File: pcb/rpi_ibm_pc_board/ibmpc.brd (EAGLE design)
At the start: 56 x 65 mm, 31 parts, among them IC1 STM32F072C8T6, SW4 324_SW, U1 MAX3232

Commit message: clean up
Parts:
- added R10, R7, R8, R9: 2K, SparkFun-Passives:0805
- added R3, R4: 5.1k, SparkFun-Passives:0805
- added R5: 12K, SparkFun-Passives:0805
- added SW1: 324_SW, 3pos_slide_switch_centered:342_SWICH_FOOT
- added U$6: MCP4451, ps2:TSSOP20
- moved JP4 41.8 mm to (51.7, 53.9), turned to 0 degrees
- moved C2 30.0 mm to (10.9, 20.0)
- moved SW4 27.5 mm to (14.7, 38.5), turned to 180 degrees
- moved C3 21.4 mm to (12.1, 9.98)
- moved C1 15.1 mm to (15.4, 17.9)
- moved R1 14.9 mm to (9.19, 16.4)
- moved J3 9.50 mm to (52.0, 23.0)
- moved J4 8.18 mm to (48.0, 45.1)
- moved U1 6.23 mm to (40.4, 24.7), turned to 270 degrees
- moved IC1 2.02 mm to (29.1, 36.7), turned to 270 degrees
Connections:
- new net +UB: R10.2, R7.2, R8.2, R9.2, U$1.1, U$1.8, U$1.9
- new net N$1: J4.A5, R3.1
- new net N$12: IC1.31, JP4.3
- new net N$14: IC1.30, JP4.4
- new net N$15: IC1.34, JP4.1
- new net N$16: IC1.37, JP4.2
- new net N$17: R7.1, U$1.2
- new net N$18: IC1.44, R5.2, SW1.P$1, SW1.P$4
- new net N$19: R8.1, U$1.7
- new net N$20: R9.1, U$1.10
- new net N$21: R10.1, U$1.14
- new net N$7: J4.B5, R4.1
- new net N$8: IC1.33, J4.A6, J4.B6
- new net N$9: IC1.32, J4.A7, J4.B7
- new net SPI_CS: IC1.14, JP1.24
- new net SPI_MISO: IC1.16, JP1.21
- new net SPI_MOSI: IC1.17, JP1.19
- new net SPI_SCK: IC1.15, JP1.23
- net +3V3: now also JP4.6, SW1.P$2, SW1.P$3
- net GND: now also J4.GND, J4.GND2, J4.SHLD1, J4.SHLD2, J4.SHLD3, J4.SHLD4, J4.SHLD5, J4.SHLD6, J4.SHLD7, J4.SHLD8, JP4.5, R3.2, R4.2, R5.1, U$1.4, U$1.5
- net N$13: now also IC1.7

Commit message: working on IBM PC p board
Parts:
- moved R4 81.5 mm to (53.9, 46.4), turned to 180 degrees
- moved R3 77.0 mm to (50.4, 46.4), turned to 180 degrees
- moved R2 72.8 mm to (64.6, 75.2)
- moved LED1 72.8 mm to (64.5, 72.7)
- moved LED2 72.8 mm to (65.7, 62.7)
- moved R6 72.8 mm to (69.8, 62.7)
- moved R5 64.6 mm to (12.2, 47.5), turned to 180 degrees
- moved C3 34.9 mm to (17.6, 44.4), turned to 270 degrees
- moved C2 29.0 mm to (27.5, 43.8), turned to 270 degrees
- moved C6 24.6 mm to (32.4, 35.8), turned to 180 degrees
- moved R1 20.8 mm to (12.2, 37.0), turned to 0 degrees
- moved C9 20.1 mm to (30.0, 32.6), turned to 270 degrees
- moved JP4 19.5 mm to (35.7, 42.8), turned to 270 degrees
- moved C1 19.4 mm to (26.6, 33.7), turned to 270 degrees
- moved C4 18.6 mm to (30.0, 29.6), turned to 270 degrees
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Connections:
- removed net VBAT: IC1.1
- removed net VDDA: IC1.9
- removed net VDD_1: IC1.24
- removed net VDD_2: IC1.36
- removed net VDD_3: IC1.48
- removed net VSSA: IC1.8
- removed net VSS_1: IC1.23
- removed net VSS_2: IC1.35
- removed net VSS_3: IC1.47
- new net N$22: IC1.42, JP1.5
- new net N$23: IC1.43, JP1.3
- new net N$24: IC1.25, U1.10
- new net N$25: J3.8, U1.7
- new net PC_RTS: IC1.19, U1.9
- new net RTS_HV: J3.7, U1.8
- new net STM32_RX: IC1.22, U1.12
- new net STM32_RX_HV: J3.3, U1.13
- new net STM32_TX: IC1.21, U1.11
- new net STM32_TX_HV: J3.2, U1.14
- net +3V3: now also IC1.1, IC1.24, IC1.36, IC1.48, IC1.9, JP4.4; no longer JP4.6
- net GND: now also IC1.23, IC1.35, IC1.47, IC1.8, JP4.3; no longer JP4.5
- net N$12: now also JP4.5; no longer JP4.3
- net N$13: now also JP1.22
- net N$14: now also JP4.6; no longer JP4.4
- net N$18: now also JP1.32
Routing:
- net N$24: track 0.00 -> 52.8 mm
- net GND: track 0.00 -> 32.8 mm
- net RTS_HV: track 0.00 -> 31.5 mm
- net N$9: track 0.00 -> 31.3 mm
- net N$25: track 0.00 -> 31.0 mm
- net N$8: track 0.00 -> 30.5 mm
- net STM32_TX: track 0.00 -> 26.0 mm
- net STM32_RX: track 0.00 -> 25.7 mm
- net PC_RTS: track 0.00 -> 24.7 mm
- net SPI_MOSI: track 0.00 -> 22.1 mm
- net N$18: track 0.00 -> 21.3 mm
- net SPI_SCK: track 0.00 -> 20.5 mm
- net SPI_MISO: track 0.00 -> 20.4 mm
- net +3V3: track 0.00 -> 18.8 mm, vias 0 -> 4
- net SPI_CS: track 0.00 -> 17.1 mm
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
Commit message: ibm card done
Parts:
- removed JP11, JP2, JP3, JP9: (no value), pinhead:1X04
- added C8: 100nF, clock:0805@1
- added LED3: (no value), adafruit:CHIP-LED0805
- added R11, R12: 2K, SparkFun-Passives:0805
- added TP1, TP2, TP3, TP4: TPTP12R, testpad:TP12R
- added U$7, U$8, U$9: PINHD1X4, adafruit_changed:1X04-CLEANBIG
- JP4: device pinhead:2X03 -> pinhead:2X04
- moved R6 56.4 mm to (50.2, 9.83), turned to 270 degrees
- moved LED2 54.5 mm to (52.7, 9.78), turned to 180 degrees
- moved R2 47.5 mm to (26.5, 46.7), turned to 0 degrees
- moved LED1 44.8 mm to (26.5, 49.0)
- moved JP4 2.51 mm to (38.1, 43.4)
- moved U$6 2.44 mm to (18.4, 24.9), turned to 180 degrees
- moved C6 1.94 mm to (34.4, 36.0), turned to 0 degrees
- moved R9 1.02 mm to (23.4, 13.8)
- moved C7 0.92 mm to (40.0, 34.4), turned to 90 degrees
- moved R7 0.70 mm to (19.1, 13.8)
- moved R8 0.68 mm to (38.1, 13.8)
- moved R10 0.57 mm to (34.5, 13.8), turned to 180 degrees
- moved R5 0.51 mm to (12.2, 48.0)
- moved SW1 0.51 mm to (12.2, 45.1)
- moved SW4 0.51 mm to (12.2, 40.4)
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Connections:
- new net N$26: IC1.40, J1.1_DATA, U$7.2
- new net N$27: IC1.38, JP4.1, R11.1
- new net N$28: LED3.A, R11.2
- new net N$30: IC1.27, U$6.6
- new net N$31: IC1.26, U$6.5
- new net N$32: R12.1, U$6.4
- new net N$33: U$1.3, U$6.12
- new net N$34: U$1.11, U$6.9
- new net N$35: U$1.6, U$6.19
- new net N$36: U$1.13, U$6.2
- new net N$37: IC1.2, JP1.36
- new net N$38: IC1.10, U$9.1
- new net N$39: IC1.11, U$9.2
- new net N$40: IC1.12, U$9.3
- new net N$41: IC1.13, U$9.4
- new net N$42: IC1.29, TP1.TP
- new net N$43: IC1.28, TP2.TP
- new net N$44: IC1.20, TP4.TP
- new net N$45: IC1.18, TP3.TP
- net +3V3: now also C8.2, JP4.6, U$6.17; no longer JP11.1, JP11.2, JP11.3, JP11.4, JP4.4, LED1.A
- net +UB: now also U$6.1, U$6.10, U$6.11, U$6.20
- net GND: now also C8.1, JP4.5, LED1.C, LED3.C, R12.2, U$1.G1, U$1.G2, U$6.16, U$6.7, U$7.4, U$8.4; no longer JP2.1, JP3.1, JP4.3, JP9.1, JP9.2, JP9.3, JP9.4
- net N$10: now also IC1.45, U$8.2; no longer JP3.3
- net N$11: now also IC1.46, U$8.3; no longer JP3.2
- net N$12: now also JP4.7; no longer JP4.5
- net N$14: now also JP4.8; no longer JP4.6
- net N$15: now also JP4.3; no longer JP4.1
- net N$16: now also JP4.4; no longer JP4.2
- net N$17: now also IC1.3
- net N$19: now also IC1.5
- net N$2: now also LED1.A; no longer LED1.C
- net N$20: now also IC1.4
- net N$21: now also IC1.6
- net N$3: now also U$7.1; no longer JP2.4
- net N$4: now also U$8.1; no longer JP3.4
- net N$5: now also IC1.41, U$7.3; no longer JP2.2
- net N$6: now also IC1.39, JP4.2, R2.1; no longer J1.1_DATA, JP2.3
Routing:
- net +UB: track 0.00 -> 82.8 mm
- net N$22: track 0.00 -> 53.5 mm, vias 0 -> 1
- net N$21: track 0.00 -> 53.3 mm, vias 0 -> 1
- net N$23: track 0.00 -> 51.2 mm, vias 0 -> 1
- net N$19: track 0.00 -> 48.7 mm, vias 0 -> 1
- net N$36: track 0.00 -> 48.2 mm
- net N$20: track 0.00 -> 43.7 mm, vias 0 -> 1
- net N$17: track 0.00 -> 42.5 mm, vias 0 -> 1
- net N$34: track 0.00 -> 35.4 mm
- net N$26: track 0.00 -> 32.2 mm
- net N$6: track 0.00 -> 25.6 mm
- net N$5: track 0.00 -> 25.4 mm
- net N$37: track 0.00 -> 23.7 mm
- net N$33: track 0.00 -> 19.3 mm
- net N$35: track 0.00 -> 17.6 mm
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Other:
- board text added: "3V"
- board text added: "A0"
- board text added: "A1"
- board text added: "A14"
- board text added: "A15"
- board text added: "A2"
- board text added: "A3"
- board text added: "A8"
- board text added: "ACT"
- board text added: "AT/PS2 KB"
- board text added: "B0"
- board text added: "B15"
- board text added: "B2"
- board text added: "DFU"
- board text added: "ERR"
- board text added: "PS/2 MOUSE"
- board text added: "RST"
- board text added: "RX"
- board text added: "SERIAL MOUSE"
- board text added: "USB4VC Protocol Board for IBM PC Compatibles"
- board text added: "USE STRAIGHT-THRU DB9 RS232 CABLE"
- board text added: "git.io/usb4vc"
- board text added: "git.io/usb4vc PT1 dekuNukem Dec 2021"
- board text removed: "3V3"
- board text removed: "CS"
- board text removed: "KEYBOARD"
- board text removed: "MISO"
- board text removed: "MOSI"
- board text removed: "MOUSE"
- board text removed: "PA2"
- board text removed: "PA3"
- board text removed: "R1IN"
- board text removed: "R1OUT"
- board text removed: "R2IN"
- board text removed: "R2OUT"
- board text removed: "SCK"
- board text removed: "STM32 RST"
- board text removed: "S_REQ"
- board text removed: "T1IN"
- board text removed: "T1OUT"
- board text removed: "T2IN"
- board text removed: "T2OUT"
- board text removed: "U2R PS2 PT1 Nov21 dekuNukem"
- board text removed: "USE STRAIGHT-THROUGH DB9 RS232 CABLE"

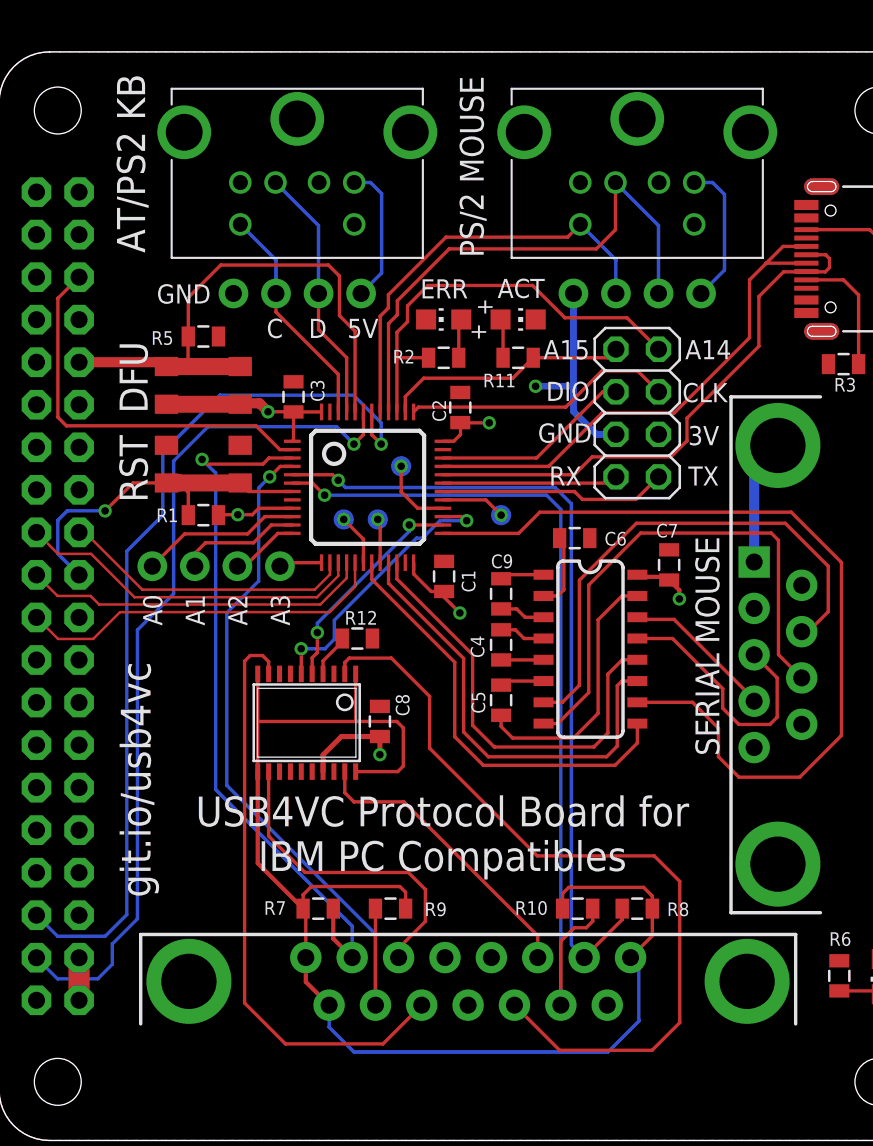
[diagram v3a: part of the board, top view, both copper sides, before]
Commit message: added i2c pullups, cleanup
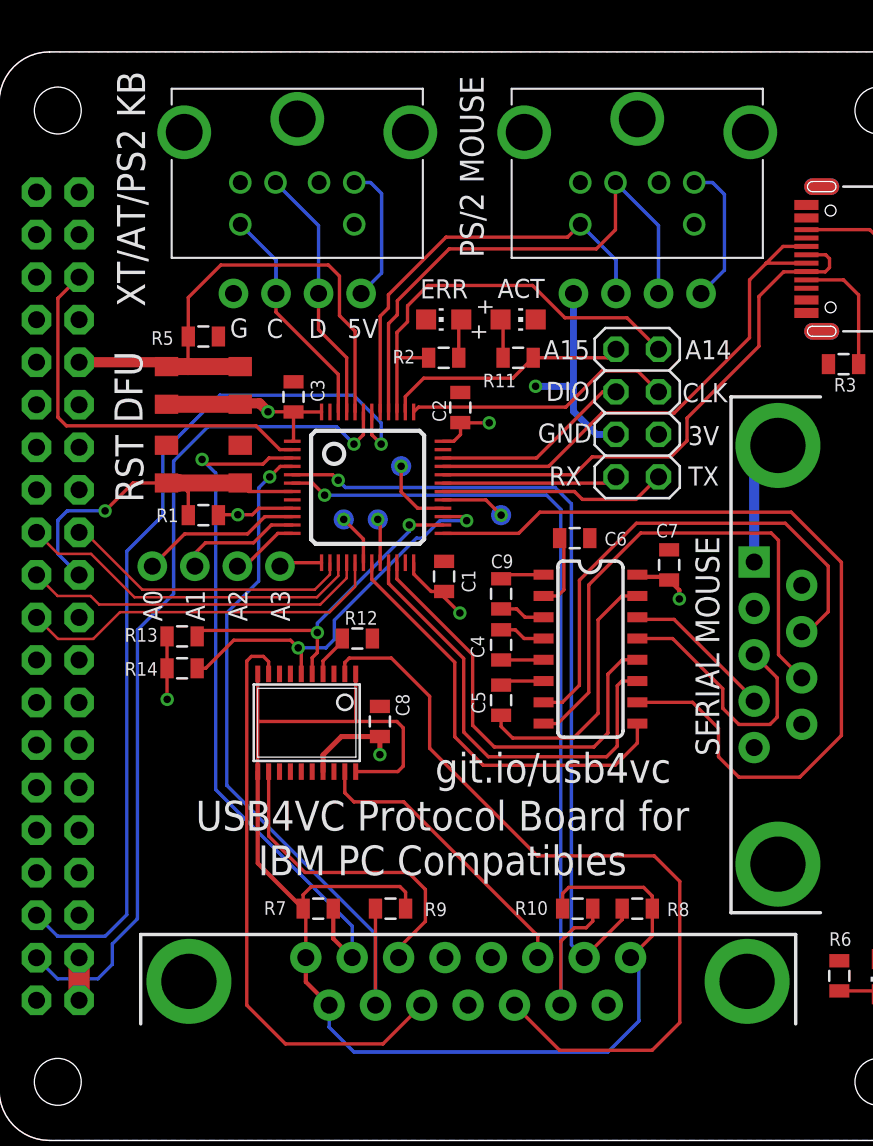
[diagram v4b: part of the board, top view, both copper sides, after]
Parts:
- added R13, R14: 5.1k, SparkFun-Passives:0805
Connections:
- net +3V3: now also R13.1, R14.1
- net N$30: now also R14.2
- net N$31: now also R13.2
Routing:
- net N$31: track 13.3 -> 20.7 mm
- net N$30: track 16.7 -> 23.9 mm
- net +3V3: track 35.2 -> 39.0 mm, vias 7 -> 8
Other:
- board text added: "G"
- board text added: "XT/AT/PS2 KB"
- board text removed: "AT/PS2 KB"
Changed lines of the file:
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@@
 <wire x1="0" y1="62" x2="0" y2="3" width="0" layer="20"/>
 <wire x1="0" y1="3" x2="3" y2="0" width="0" layer="20" curve="90"/>
-<text x="26.4668" y="18.3134" size="1.778" layer="25" rot="R180" align="center">USB4VC Protocol Board for
+<text x="26.4668" y="18.0594" size="1.778" layer="25" rot="R180" align="center">USB4VC Protocol Board for
 IBM PC Compatibles</text>
 <text x="42.0624" y="42.0878" size="1.143" layer="25" rot="R180" align="center">3V</text>
@@
 <text x="42.3418" y="47.2186" size="1.143" layer="25" rot="R180" align="center">A14</text>
 <text x="33.8836" y="47.2186" size="1.143" layer="25" rot="R180" align="center">A15</text>
-<text x="7.874" y="58.3438" size="1.6764" layer="25" rot="R270" align="center">AT/PS2 KB</text>
+<text x="7.874" y="56.8198" size="1.6764" layer="25" rot="R270" align="center">XT/AT/PS2 KB</text>
 <text x="28.2194" y="58.1406" size="1.4224" layer="25" rot="R90" align="center">PS/2 MOUSE</text>
-<text x="11.0236" y="50.546" size="1.143" layer="25" align="center">GND</text>
+<text x="14.3256" y="48.514" size="1.143" layer="25" align="center">G</text>
 <text x="21.717" y="48.4886" size="1.143" layer="25" align="center">5V</text>
 <text x="19.0246" y="48.4886" size="1.143" layer="25" align="center">D</text>
 <text x="16.4592" y="48.4886" size="1.143" layer="25" align="center">C</text>
 <text x="54.7624" y="10.1092" size="1.143" layer="25" rot="R270" align="center">POWER</text>
-<text x="8.0264" y="40.1066" size="1.6764" layer="25" rot="R270" align="center">RST</text>
+<text x="7.7724" y="40.1066" size="1.6764" layer="25" rot="R270" align="center">RST</text>
 <text x="52.197" y="29.0068" size="1.4224" layer="26" rot="MR270" align="center">USE STRAIGHT-THRU
 DB9 RS232 CABLE
@@
 <text x="33.8074" y="39.6748" size="1.143" layer="25" rot="R180" align="center">RX</text>
 <text x="42.0624" y="39.6748" size="1.143" layer="25" rot="R180" align="center">TX</text>
-<text x="8.0264" y="45.5676" size="1.6764" layer="25" rot="R270" align="center">DFU</text>
-<text x="9.1694" y="31.6738" size="1.143" layer="25" rot="R270" align="center">A0</text>
-<text x="11.7094" y="31.6738" size="1.143" layer="25" rot="R270" align="center">A1</text>
-<text x="14.2494" y="31.6738" size="1.143" layer="25" rot="R270" align="center">A2</text>
-<text x="16.7894" y="31.6738" size="1.143" layer="25" rot="R270" align="center">A3</text>
+<text x="7.7216" y="44.9834" size="1.6764" layer="25" rot="R90" align="center">DFU</text>
+<text x="9.1694" y="31.9278" size="1.143" layer="25" rot="R270" align="center">A0</text>
+<text x="11.7094" y="31.9278" size="1.143" layer="25" rot="R270" align="center">A1</text>
+<text x="14.2494" y="31.9278" size="1.143" layer="25" rot="R270" align="center">A2</text>
+<text x="16.7894" y="31.9278" size="1.143" layer="25" rot="R270" align="center">A3</text>
 <text x="26.289" y="40.259" size="1.143" layer="26" rot="MR0" align="center">B15</text>
 <text x="31.7246" y="37.3126" size="1.143" layer="26" rot="MR0" align="center">A8</text>
@@
 <text x="28" y="3.81" size="1.6764" layer="26" rot="MR180" align="center">git.io/usb4vc
 PT1 dekuNukem Dec 2021</text>
-<text x="8.1534" y="21.5392" size="1.778" layer="25" rot="R90" align="center">git.io/usb4vc</text>
+<text x="33.0708" y="22.2504" size="1.778" layer="25" rot="R180" align="center">git.io/usb4vc</text>
 </plain>
 <attributes>
@@
 <attribute name="TP_SIGNAL_NAME" value="" x="22.606" y="37.084" size="1.778" layer="28" rot="MR0" display="off"/>
 </element>
+<element name="R13" library="SparkFun-Passives" package="0805" value="5.1k" x="10.922" y="30.099" smashed="yes">
+<attribute name="NAME" x="7.493" y="29.7815" size="0.8128" layer="25"/>
+</element>
+<element name="R14" library="SparkFun-Passives" package="0805" value="5.1k" x="10.922" y="28.194" smashed="yes">
+<attribute name="NAME" x="7.493" y="27.7495" size="0.8128" layer="25"/>
+</element>
 </elements>
 <signals>
@@
 <wire x1="40.005" y1="33.4662" x2="40.6146" y2="32.8566" width="0.254" layer="1"/>
 <wire x1="40.6146" y1="32.8566" x2="40.6146" y2="32.3342" width="0.254" layer="1"/>
+<contactref element="R13" pad="1"/>
+<contactref element="R14" pad="1"/>
+<via x="10.033" y="26.3398" extent="1-16" drill="0.45"/>
+<wire x1="10.033" y1="26.3398" x2="10.022" y2="26.3508" width="0.2032" layer="1"/>
+<wire x1="10.022" y1="26.3508" x2="10.022" y2="28.194" width="0.2032" layer="1"/>
+<wire x1="10.022" y1="28.194" x2="10.022" y2="30.099" width="0.2032" layer="1"/>
 </signal>
 <signal name="N$29">
@@
 <wire x1="27.6724" y1="37.25" x2="27.9146" y2="37.0078" width="0.2032" layer="1"/>
 <via x="27.9146" y="37.0078" extent="1-16" drill="0.45"/>
-<via x="18.034" y="29.3624" extent="1-16" drill="0.45"/>
-<wire x1="18.034" y1="29.3624" x2="18.0392" y2="29.3572" width="0.2032" layer="1"/>
-<wire x1="18.0392" y1="29.3572" x2="18.0392" y2="27.8606" width="0.2032" layer="1"/>
+<via x="17.8562" y="29.4132" extent="1-16" drill="0.45"/>
+<wire x1="17.8562" y1="29.4132" x2="18.0392" y2="29.2302" width="0.2032" layer="1"/>
+<wire x1="18.0392" y1="29.2302" x2="18.0392" y2="27.8606" width="0.2032" layer="1"/>
 <wire x1="27.9146" y1="37.0078" x2="26.3144" y2="37.0078" width="0.2032" layer="16"/>
 <wire x1="26.3144" y1="37.0078" x2="25.273" y2="35.9664" width="0.2032" layer="16"/>
 <wire x1="25.273" y1="35.9664" x2="24.9174" y2="35.9664" width="0.2032" layer="16"/>
 <wire x1="20.0152" y1="31.0642" x2="20.0152" y2="29.9212" width="0.2032" layer="16"/>
-<wire x1="20.0152" y1="29.9212" x2="19.4564" y2="29.3624" width="0.2032" layer="16"/>
-<wire x1="19.4564" y1="29.3624" x2="18.034" y2="29.3624" width="0.2032" layer="16"/>
+<wire x1="20.0152" y1="29.9212" x2="19.5072" y2="29.4132" width="0.2032" layer="16"/>
+<wire x1="19.5072" y1="29.4132" x2="17.8562" y2="29.4132" width="0.2032" layer="16"/>
 <wire x1="24.9174" y1="35.9664" x2="20.0152" y2="31.0642" width="0.2032" layer="16"/>
+<contactref element="R14" pad="2"/>
+<wire x1="17.8562" y1="29.4132" x2="17.399" y2="29.8704" width="0.2032" layer="1"/>
+<wire x1="17.399" y1="29.8704" x2="14.0064" y2="29.8704" width="0.2032" layer="1"/>
+<wire x1="14.0064" y1="29.8704" x2="12.33" y2="28.194" width="0.2032" layer="1"/>
+<wire x1="12.33" y1="28.194" x2="11.822" y2="28.194" width="0.2032" layer="1"/>
 </signal>
 <signal name="N$31">
@@
 <wire x1="18.6892" y1="28.8238" x2="18.6892" y2="27.8606" width="0.2032" layer="1"/>
 <wire x1="18.9992" y1="29.1338" x2="18.6892" y2="28.8238" width="0.2032" layer="1"/>
+<contactref element="R13" pad="2"/>
+<wire x1="18.9992" y1="30.3276" x2="18.8722" y2="30.4546" width="0.2032" layer="1"/>
+<wire x1="18.8722" y1="30.4546" x2="12.1776" y2="30.4546" width="0.2032" layer="1"/>
+<wire x1="12.1776" y1="30.4546" x2="11.822" y2="30.099" width="0.2032" layer="1"/>
 </signal>
 <signal name="N$32">
@@
 <wire x1="25.23" y1="8.08" x2="22.9158" y2="5.7658" width="0.2032" layer="1"/>
 <wire x1="22.9158" y1="5.7658" x2="17.0942" y2="5.7658" width="0.2032" layer="1"/>
-<wire x1="17.0942" y1="5.7658" x2="14.6558" y2="8.2042" width="0.2032" layer="1"/>
-<wire x1="14.6558" y1="8.2042" x2="14.6558" y2="28.6258" width="0.2032" layer="1"/>
-<wire x1="14.6558" y1="28.6258" x2="14.986" y2="28.956" width="0.2032" layer="1"/>
-<wire x1="15.7226" y1="28.956" x2="16.0892" y2="28.5894" width="0.2032" layer="1"/>
-<wire x1="14.986" y1="28.956" x2="15.7226" y2="28.956" width="0.2032" layer="1"/>
+<wire x1="17.0942" y1="5.7658" x2="14.7828" y2="8.0772" width="0.2032" layer="1"/>
+<wire x1="14.7828" y1="8.0772" x2="14.7828" y2="28.6258" width="0.2032" layer="1"/>
+<wire x1="14.7828" y1="28.6258" x2="15.0622" y2="28.9052" width="0.2032" layer="1"/>
+<wire x1="15.7734" y1="28.9052" x2="16.0892" y2="28.5894" width="0.2032" layer="1"/>
+<wire x1="15.0622" y1="28.9052" x2="15.7734" y2="28.9052" width="0.2032" layer="1"/>
 </signal>
 <signal name="N$36">
